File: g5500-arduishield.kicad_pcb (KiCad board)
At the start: 2 copper layers, 68.6 x 53.3 mm, 23 parts, among them Q1 PN2222A, Q2 PN2222A, Q3 PN2222A, Q4 PN2222A

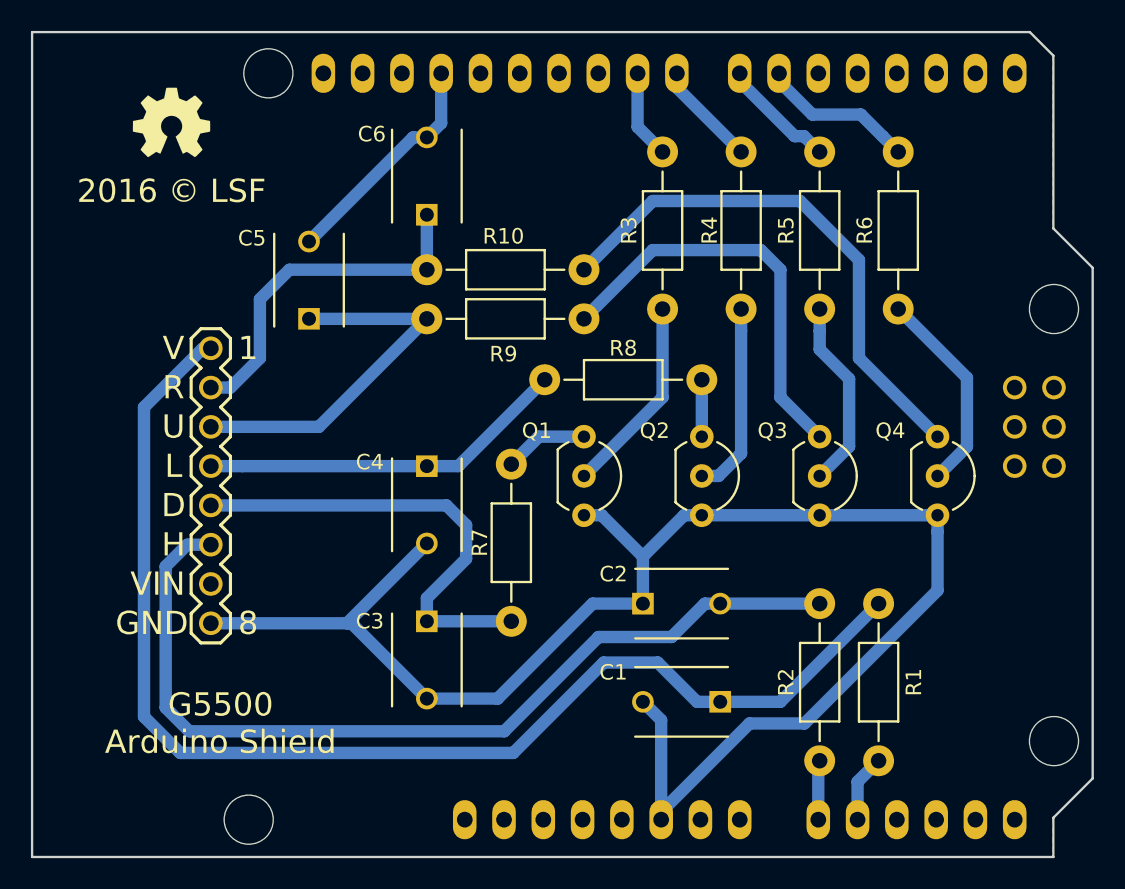
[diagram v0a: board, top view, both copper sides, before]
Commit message: Add slight routing adjustments and addition of F.Cu GND zone
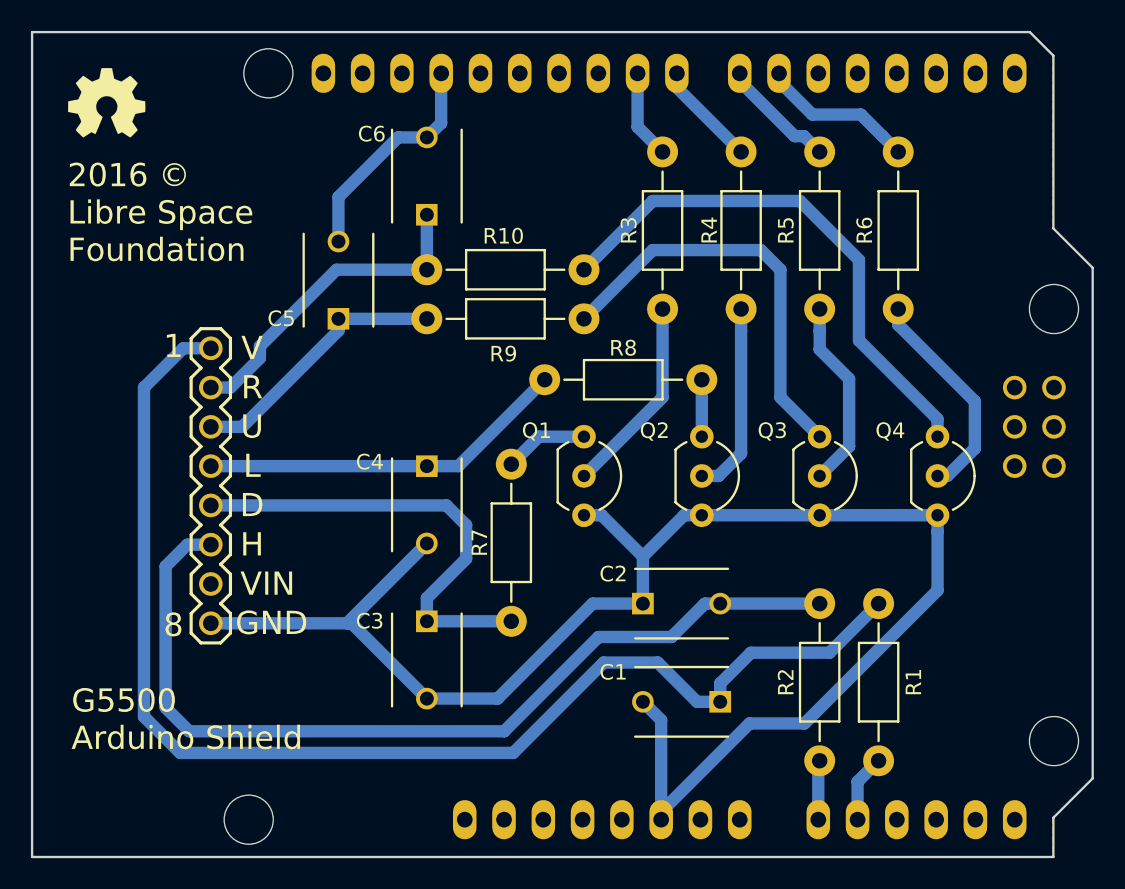
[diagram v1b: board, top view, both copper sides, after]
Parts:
- moved LOGO_OSHW_silkscreen_5mm 4.38 mm to (122.2, 73.7)
- moved C5 1.91 mm to (137.2, 87.6)
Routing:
- net U: track 24.5 -> 17.3 mm
- net R: track 22.9 -> 21.1 mm
- net H: track 80.5 -> 81.9 mm
- net Net-(Q4-Pad2): track 13.4 -> 14.2 mm
- added copper zone on F.Cu, net GND
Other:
- board text added: "2016 © Libre Space Foundation"
- board text removed: "2016 © LSF"
